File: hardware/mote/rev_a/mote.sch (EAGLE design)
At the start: 70 parts, among them Q1 CSD22206W, Q2 CSD75207W15, Q3 CSD75207W15, Q4 CSD13303W1015, Q5 CSD22206W, U1 NRF52840, U10 MS5637-02BA03, U3 MAX17222, U5 SI7021-A20-GM1, U6 ISL29125, U7 MAX44009, U8 LIS2DW12, U9 AB1815-T3, X1 7V-32.000MAHV-T, X3 ABS07-32.768KHZ-7-T

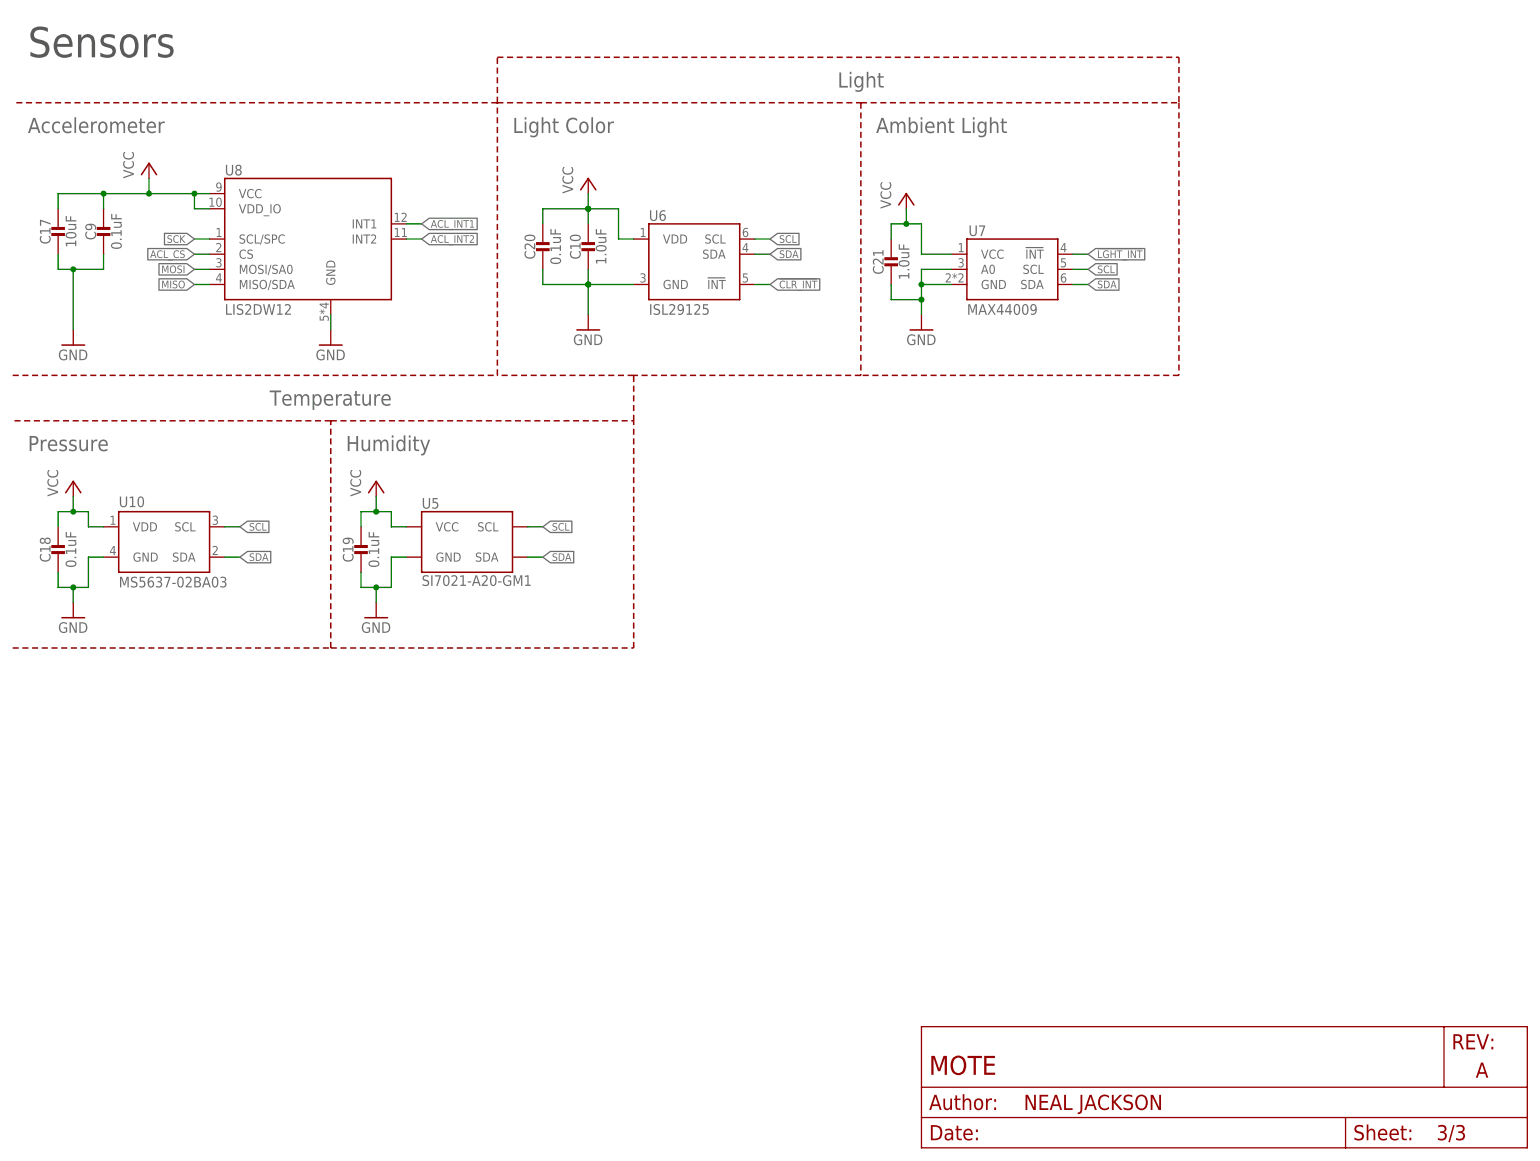
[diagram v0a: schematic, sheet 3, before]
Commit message: Connect all gpio, add pir
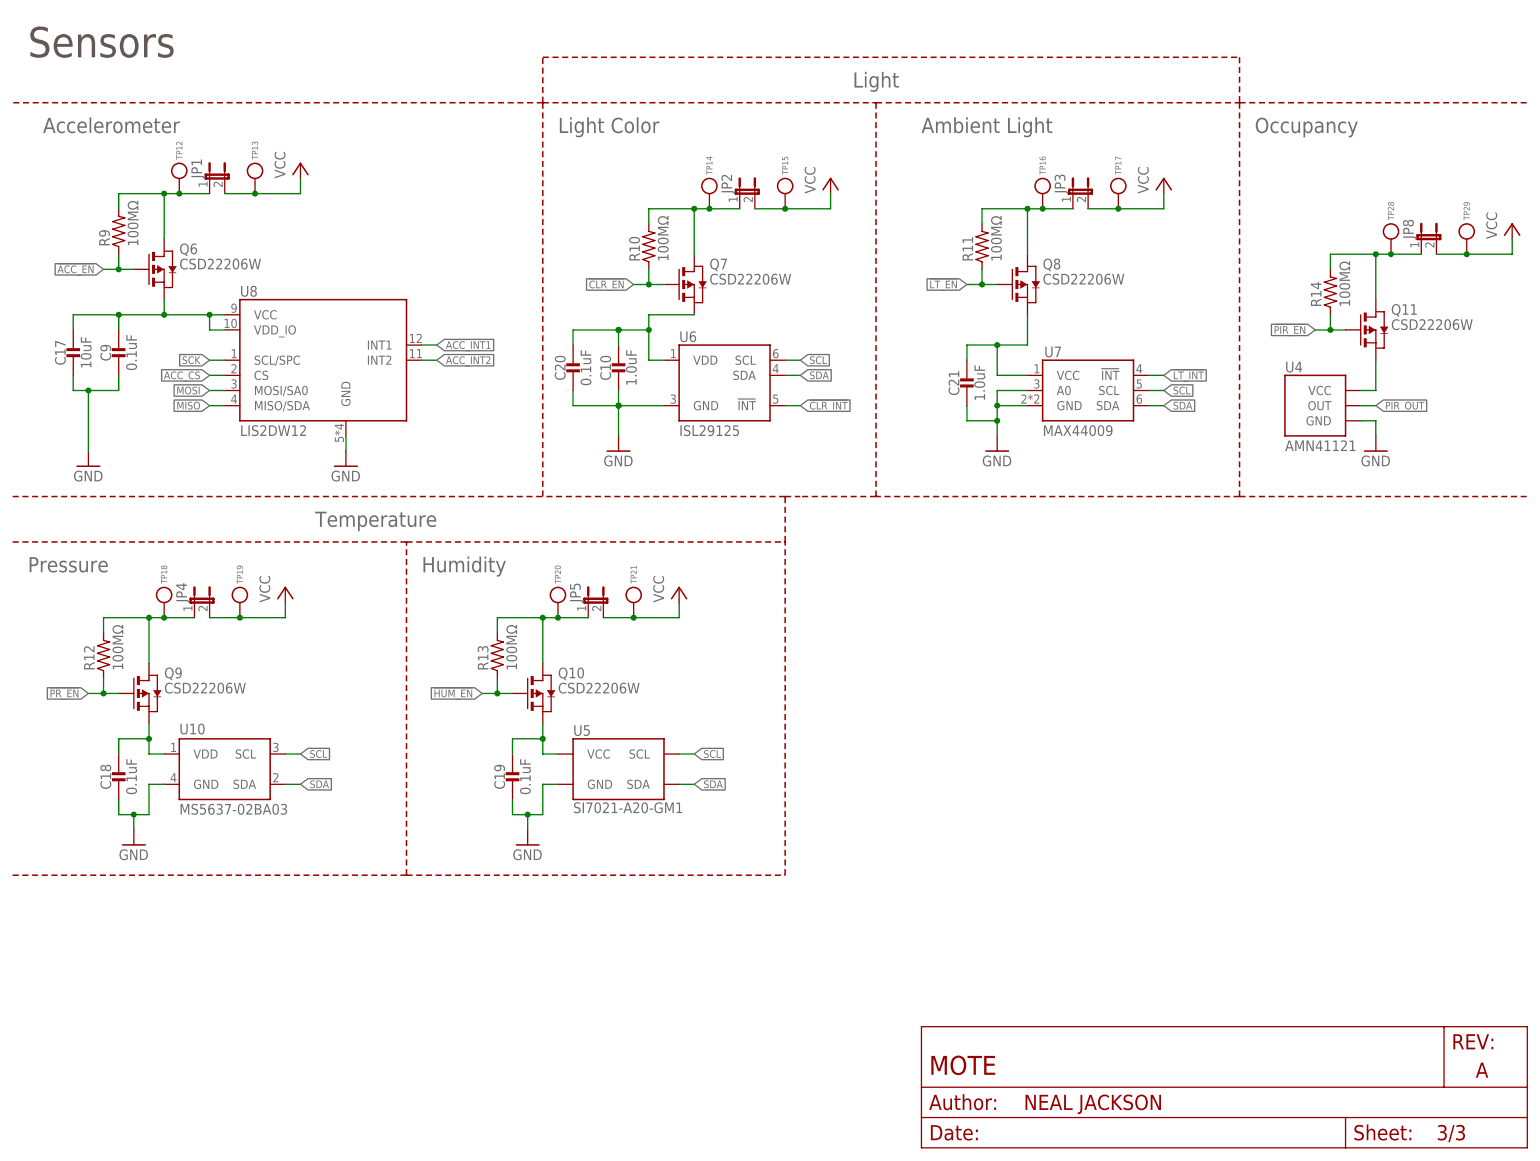
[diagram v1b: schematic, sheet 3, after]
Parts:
- added J1: TC2030-JLINK-L, connector:TC2030-JLINK-L
- added JP1, JP2, JP3, JP4, JP5, JP6, JP7, JP8: (no value), SparkFun-Passives:JUMPER-2SMD-NC
- added Q10, Q11, Q6, Q7, Q8, Q9: CSD22206W, fets:CSD22206W
- added R10, R11, R12, R13, R14, R9: 100MΩ, passives:RESISTOR0402_RES
- added TP12, TP13, TP14, TP15, TP16, TP17, TP18, TP19, TP20, TP21, TP22, TP23, TP24, TP25, TP26, TP27, TP28, TP29: TEST_POINT_0.040IN, headers:TEST_POINT_0.040IN
- added U4: AMN41121, chips:AMN41121
- R1: value 1k -> 1kΩ
- R2: value 80.6k -> 80.6kΩ
- R3: value 20 -> 20Ω
- R4: value 33M -> 33MΩ
- R5, R6: value 100k -> 100kΩ
- R7, R8: value 10k -> 10kΩ
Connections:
- removed net !LGHT_INT: U7.!INT
- removed net ACL_CS: U8.CS
- removed net ACL_INT1: U8.INT1
- removed net ACL_INT2: U8.INT2
- removed net CS_RTC: U9.!CS
- removed net ENABLE: R4.2
- removed net SW1: L3.2, TP11.TESTPOINT, U3.LX
- new net !ACC_EN: Q6.G, R9.1, U1.P1.15
- new net !CLR_EN: Q7.G, R10.1, U1.P1.14
- new net !HUM_EN: Q10.G, R13.1, U1.P1.11
- new net !LT_EN: Q8.G, R11.1, U1.P1.13
- new net !LT_INT: U1.P1.04, U7.!INT
- new net !PIR_EN: Q11.G, R14.1, U1.P1.10
- new net !PR_EN: Q9.G, R12.1, U1.P1.12
- new net ACC_CS: U1.P0.17, U8.CS
- new net ACC_INT1: U1.P1.06, U8.INT1
- new net ACC_INT2: U1.P1.07, U8.INT2
- new net N$15: C17.1, C9.1, Q6.S, U8.VCC, U8.VDD_IO
- new net N$19: C10.1, C20.1, Q7.S, U6.VDD
- new net N$20: C21.1, Q8.S, U7.VCC
- new net N$21: C18.1, Q9.S, U10.VDD
- new net N$22: C19.1, Q10.S, U5.VCC
- new net N$23: Q11.S, U4.VCC
- new net N$28: J1.SWDIO, U1.SWDIO
- new net N$29: J1.SWDCLK, U1.SWDCLK
- new net N$33: JP2.1, Q7.D, R10.2, TP14.TESTPOINT
- new net N$34: JP3.1, Q8.D, R11.2, TP16.TESTPOINT
- new net N$35: JP4.1, Q9.D, R12.2, TP18.TESTPOINT
- new net N$36: JP5.1, Q10.D, R13.2, TP20.TESTPOINT
- new net N$37: JP1.1, Q6.D, R9.2, TP12.TESTPOINT
- new net N$39: C12.1, C14.1, C6.1, C7.1, C8.1, JP7.1, TP24.TESTPOINT, U1.VDD, U1.VDDH
- new net N$42: C25.1, JP6.1, TP22.TESTPOINT, U9.VCC
- new net N$43: JP6.2, TP23.TESTPOINT
- new net PIR_OUT: U1.P1.03, U1.P1.09, U4.OUT
- new net RTC_CS: U1.P0.16, U9.!CS
- new net SW: L3.2, TP11.TESTPOINT, U1.P0.24, U3.LX
- net !CLR_INT: now also U1.P1.05
- net !RST: now also U1.P0.18; no longer U1.P0.18/RST
- net GND: now also J1.GND, TP26.TESTPOINT, TP27.TESTPOINT, U4.GND
- net MISO: now also U1.P0.15
- net MOSI: now also U1.P0.14
- net N$24: now also JP8.1, Q11.D, R14.2, TP28.TESTPOINT; no longer BAT1.+, D1.V+, Q1.D, Q2.D1, Q5.S, R1.2, TP1.TESTPOINT, U2.!DIS, U2.VCC
- net SCK: now also U1.P0.13
- net SCL: now also U1.P0.27
- net SDA: now also U1.P0.26
- net VBAT: now also U1.P0.03/AIN1; no longer C25.1, U9.VCC
- net VCC: now also J1.VCC, JP1.2, JP2.2, JP3.2, JP4.2, JP5.2, JP7.2, JP8.2, TP13.TESTPOINT, TP15.TESTPOINT, TP17.TESTPOINT, TP19.TESTPOINT, TP21.TESTPOINT, TP25.TESTPOINT, TP29.TESTPOINT; no longer C10.1, C12.1, C14.1, C17.1, C18.1, C19.1, C20.1, C21.1, C6.1, C7.1, C8.1, C9.1, U1.VDD, U1.VDDH, U10.VDD, U5.VCC, U6.VDD, U7.VCC, U8.VCC, U8.VDD_IO
- net VSW: now also BAT1.+, D1.V+, Q1.D, Q2.D1, Q5.S, R1.2, R4.2, TP1.TESTPOINT, U1.P0.02/AIN0, U2.!DIS, U2.VCC
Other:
- note added: "Occupancy"
- moved on the sheet: A1, C1, C10, C11, C12, C14, C15, C17, C18, C19, C2, C20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

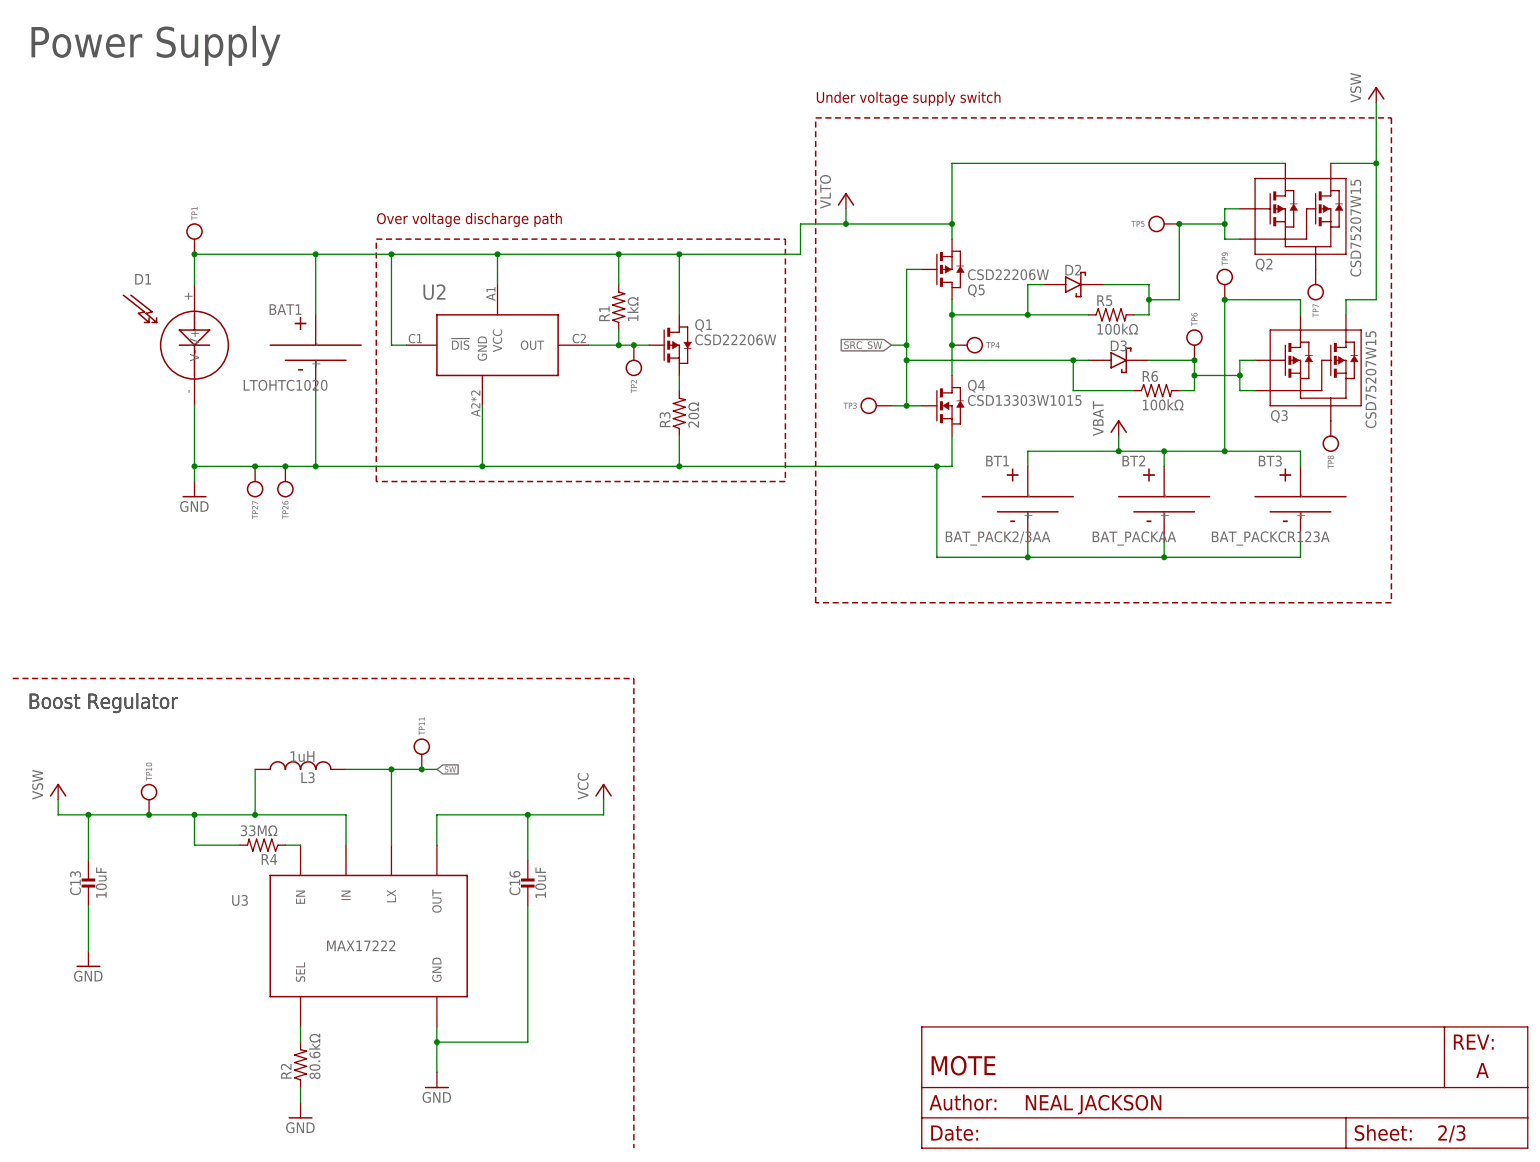
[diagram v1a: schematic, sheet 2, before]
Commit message: use mppt front end
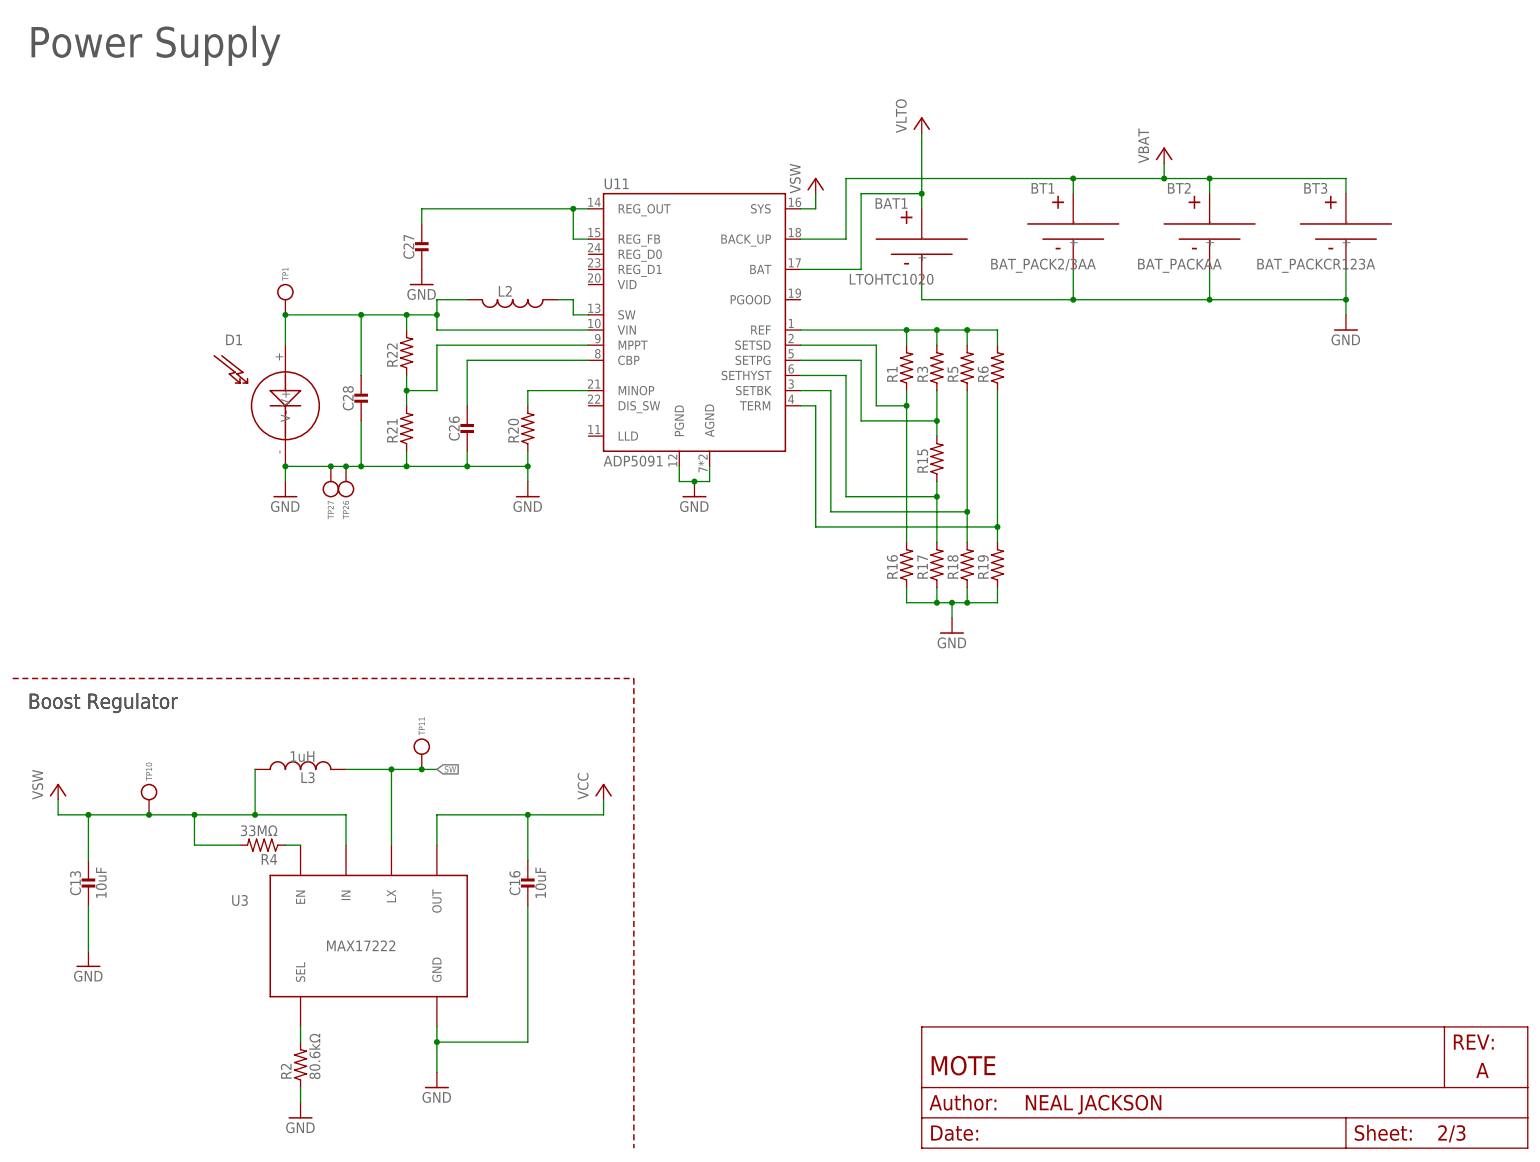
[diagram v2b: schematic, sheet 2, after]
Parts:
- removed D2, D3: DIODE_SCHOTTKYMBR0520LT1G, passives:DIODE_SCHOTTKYMBR0520LT1G
- removed Q1, Q5: CSD22206W, fets:CSD22206W
- removed Q2, Q3: CSD75207W15, fets:CSD75207W15
- removed Q4: CSD13303W1015, fets:CSD13303W1015
- removed TP2, TP3, TP4, TP5, TP6, TP7, TP8, TP9: TEST_POINT_0.040IN, headers:TEST_POINT_0.040IN
- removed U2: (no value), chips:ADM8641
- added C26, C27, C28: (no value), passives:CAPACITOR0603_CAP
- added L2: (no value), passives:INDUCTORIHL2525CZ
- added R15, R16, R17, R18, R19, R20, R21, R22: (no value), passives:RESISTOR0402_RES
- added U11: ADP5091, chips:ADP5091
- R1: value 1kΩ -> (none); DIGIKEY 311-1.0KJRCT-ND -> (none)
- R3: value 20Ω -> (none); DIGIKEY 311-20JRCT-ND -> (none)
- R5, R6: value 100kΩ -> (none); DIGIKEY 311-100KLRCT-ND -> (none)
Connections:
- removed net SRC_SW: D3.ANODE, Q4.G, Q5.G, R6.1, TP3.TESTPOINT
- new net N$30: C26.1, U11.CBP
- new net N$32: R21.2, R22.1, U11.MPPT
- new net N$38: C28.1, D1.V+, L2.2, R22.2, TP1.TESTPOINT, U11.VIN
- new net N$45: L2.1, U11.SW
- new net N$47: C27.1, U11.REG_FB, U11.REG_OUT
- net GND: now also C26.2, C27.2, C28.2, R16.1, R17.1, R18.1, R19.1, R20.1, R21.1, U11.AGND, U11.PGND; no longer Q4.S, R3.1, U2.GND
- net N$1: now also R1.1, R16.2, U11.SETSD; no longer D2.ANODE, Q4.D, Q5.D, R5.1, TP4.TESTPOINT
- net N$10: now also R1.2, R3.2, R5.2, R6.2, U11.REF; no longer Q2.S, TP7.TESTPOINT
- net N$11: now also R15.2, R3.1, U11.SETPG; no longer Q1.G, R1.1, TP2.TESTPOINT, U2.OUT
- net N$13: now also R15.1, R17.2, U11.SETHYST; no longer D2.CATHODE, Q2.G1, Q2.G2, R5.2, TP5.TESTPOINT
- net N$16: now also R18.2, R5.1, U11.SETBK; no longer Q3.S, TP8.TESTPOINT
- net N$17: now also R19.2, R6.1, U11.TERM; no longer Q1.S, R3.2
- net N$18: now also R20.2, U11.MINOP; no longer D3.CATHODE, Q3.G1, Q3.G2, R6.2, TP6.TESTPOINT
- net VBAT: now also U11.BACK_UP; no longer Q3.D1, TP9.TESTPOINT
- net VSW: now also U11.BAT, U11.SYS; no longer D1.V+, Q1.D, Q2.D1, Q2.D2, Q3.D2, Q5.S, R1.2, TP1.TESTPOINT, U2.!DIS, U2.VCC
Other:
- note removed: "Over voltage discharge path"
- note removed: "Under voltage supply switch"
- moved on the sheet: BAT1, BT1, BT2, BT3, D1, R1, R3, R5, R6, TP1, TP26, TP27
